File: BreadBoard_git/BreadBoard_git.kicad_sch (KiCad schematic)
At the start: 51 parts, among them IC1 IAUCN04S7L028ATMA1, J1 24V DC wall plug-iN, J2 LCD Driver, J3 Conn_01x15_Socket, Q1 CSD18512Q5B, Q2 CSD18512Q5B, Q3 RQ3E110AJTB, Q4 RQ3E110AJTB, Q5 RQ3E110AJTB, U1 ESP32-S3, U2 LM73605RNPR, U3 LM5148RGYR, U4 SHT45, U5 CSD17577Q5A, U6 ESP32-S3-WROOM-1

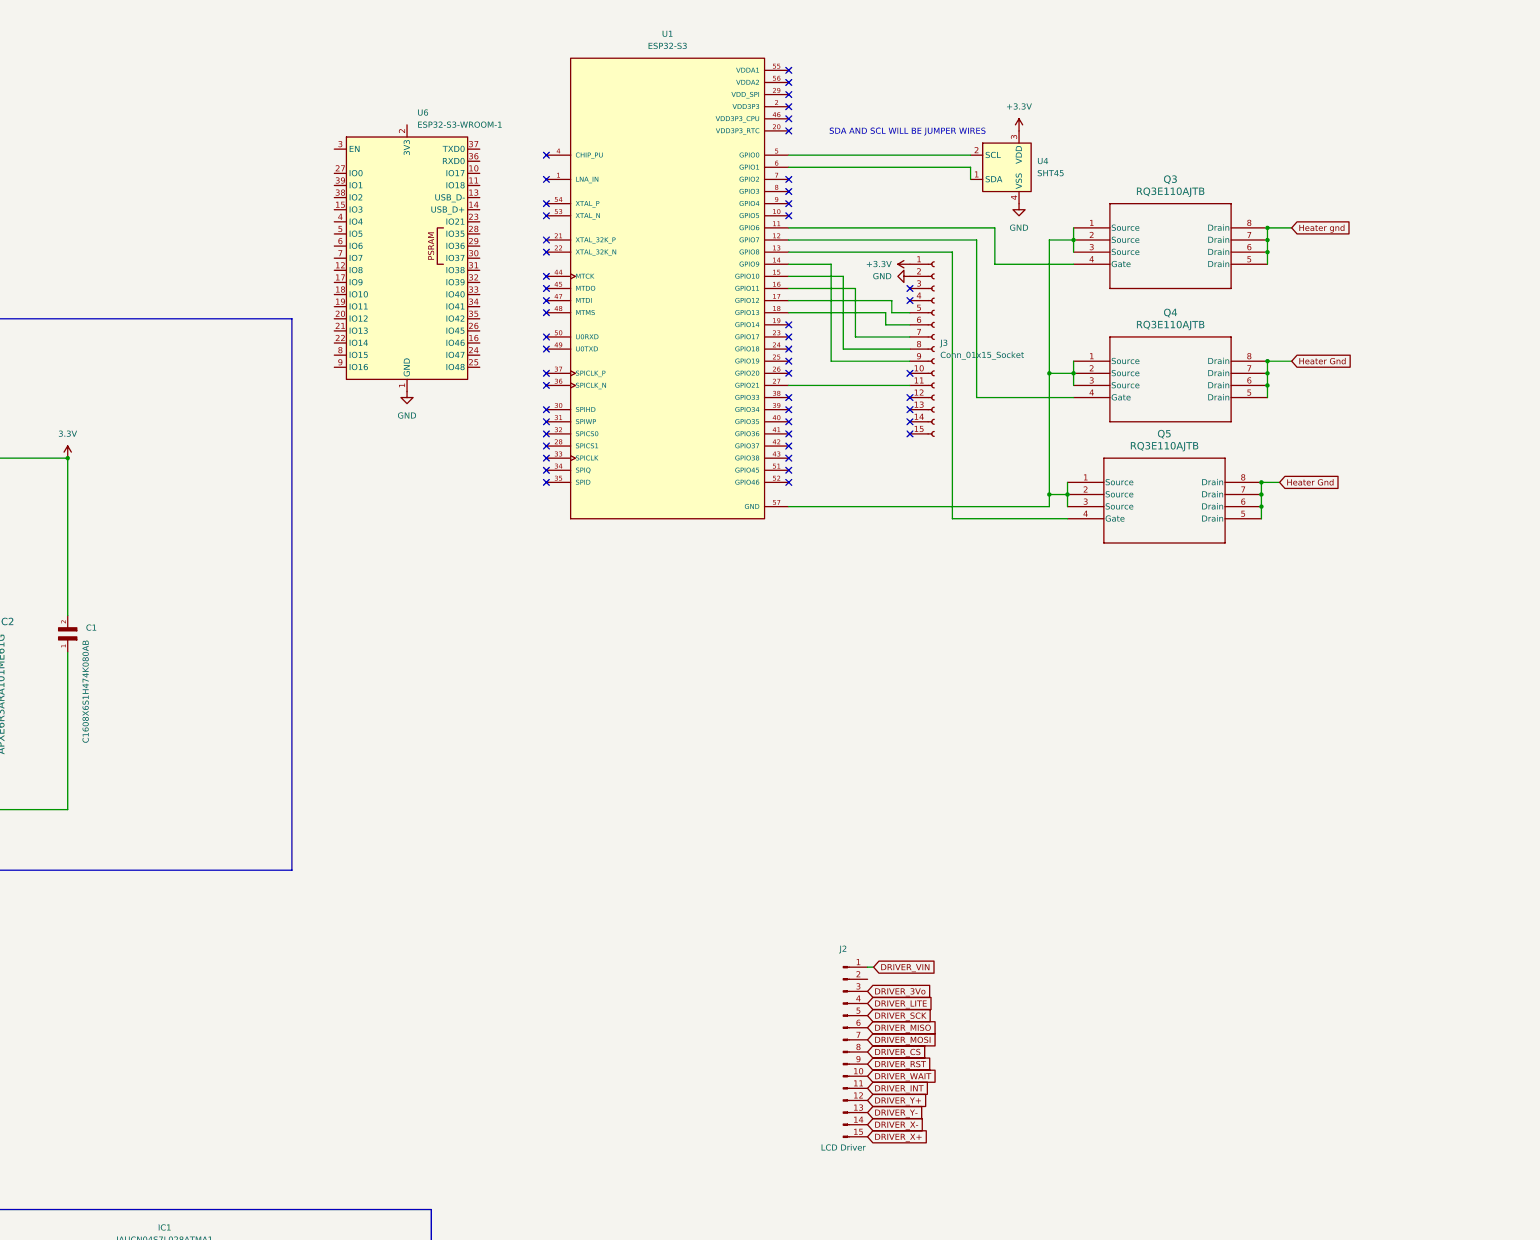
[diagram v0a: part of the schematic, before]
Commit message: 5V needs to be added
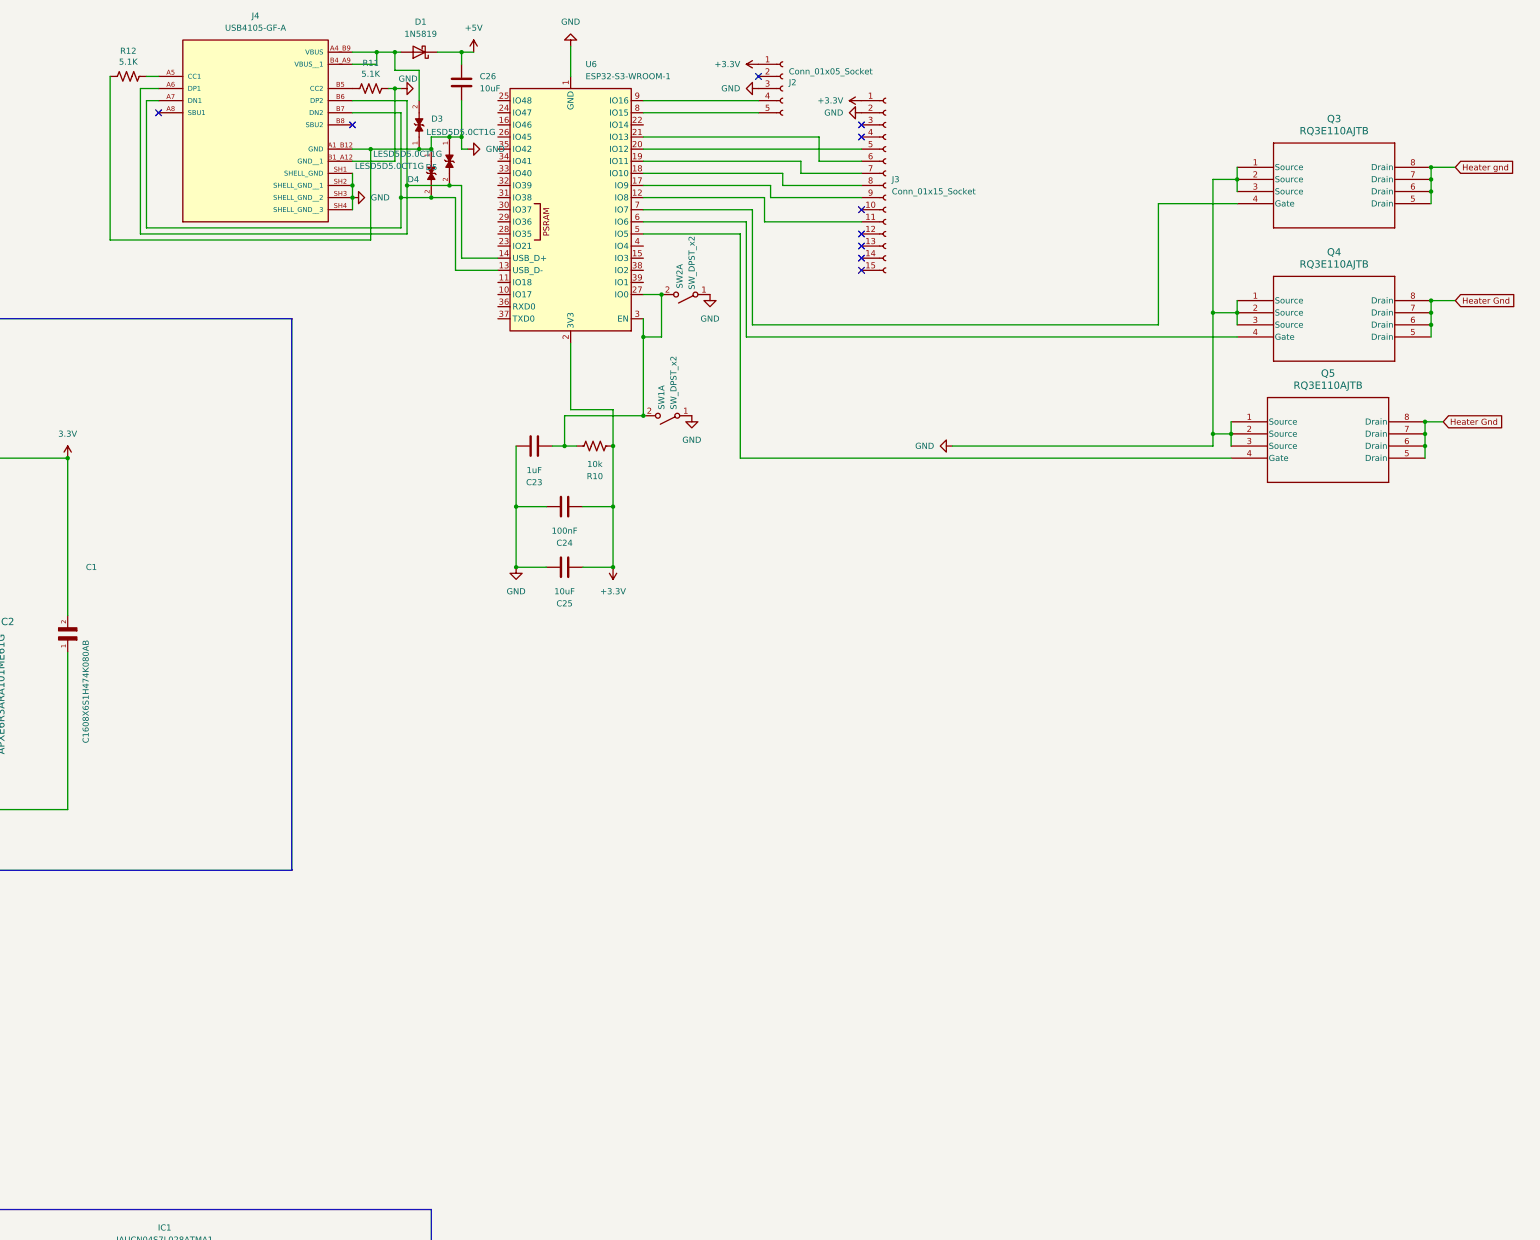
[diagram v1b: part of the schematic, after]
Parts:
- removed J2: LCD Driver, symbol Connector:Conn_01x15_Pin
- removed U1: ESP32-S3, ESP32-S3:IC_ESP32-S3, symbol ESP32-S3:ESP32-S3
- removed U4: SHT45, Sensor_Humidity:Sensirion_DFN-4_1.5x1.5mm_P0.8mm_SHT4x_NoCentralPad, symbol Sensor_Humidity:SHT4x
- added C23: 1uF, symbol Device:C
- added C24: 100nF, symbol Device:C
- added C25, C26: 10uF, symbol Device:C
- added D1: 1N5819, Diode_THT:D_DO-41_SOD81_P10.16mm_Horizontal, symbol Diode:1N5819
- added D3, D4, D5: LESD5D5.0CT1G, LESD5D5.0CT1G:TVS_LESD5D5.0CT1G, symbol LESD5D5.0CT1G:LESD5D5.0CT1G
- added J2: Conn_01x05_Socket, symbol Connector:Conn_01x05_Socket
- added J4: USB4105-GF-A, USB4105-GF-A:GCT_USB4105-GF-A, symbol USB4105-GF-A:USB4105-GF-A
- added R10: 10k, symbol Device:R_US
- added R11, R12: 5.1K, symbol Device:R_US
- added SW1, SW2: SW_DPST_x2, symbol Switch:SW_DPST_x2
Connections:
- net +3.3V: now also U6.2 (3V3), C24.1, C25.1, J2.1 (Pin_1), R10.2
- net DAP: now also Q3.1 (Source), Q3.2 (Source), Q3.3 (Source), Q4.1 (Source), Q4.2 (Source), Q4.3 (Source), Q5.1 (Source), Q5.2 (Source), Q5.3 (Source), C23.2, C24.2, C25.2, C26.2, D3.1, D4.1, D5.1, J2.3 (Pin_3), J4.A1_B12 (GND), J4.B1_A12 (GND__1), J4.SH1 (SHELL_GND), J4.SH2 (SHELL_GND__1), J4.SH3 (SHELL_GND__2), J4.SH4 (SHELL_GND__3), R11.2, R12.1, SW1.1 (A), SW2.1 (A)
- net at Q4.4 (Gate): now also U6.6 (IO6)
- net at Q5.4 (Gate): now also U6.5 (IO5)
- net at Q3.4 (Gate): now also U6.7 (IO7)
- net at J3.9 (Pin_9): now also U6.17 (IO9)
- net at J3.8 (Pin_8): now also U6.18 (IO10)
- net at J3.7 (Pin_7): now also U6.19 (IO11)
- net at J3.5 (Pin_5): now also U6.20 (IO12)
- net at J3.6 (Pin_6): now also U6.21 (IO13)
- net at J3.11 (Pin_11): now also U6.12 (IO8)
- net at U6.13 (USB_D-): now also D4.2, J4.A7 (DN1), J4.B7 (DN2)
- net at U6.14 (USB_D+): now also D5.2, J4.A6 (DP1), J4.B6 (DP2)
- net at U6.27 (IO0): now also U6.3 (EN), C23.1, R10.1, SW1.2 (B), SW2.2 (B)
- net at U6.8 (IO15): now also J2.5 (Pin_5)
- net at U6.9 (IO16): now also J2.4 (Pin_4)
- new net: J4.B5 (CC2), R11.1
- new net: D1.2 (A), D3.2, J4.A4_B9 (VBUS), J4.B4_A9 (VBUS__1)
- new net: J4.A5 (CC1), R12.2
- new net +5V: C26.1, D1.1 (K)
- no-connect marks 53 -> 12
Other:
- note removed: "SDA AND SCL WILL BE JUMPER WIRES"
- moved on the sheet: J3, Q3, Q4, Q5, U6

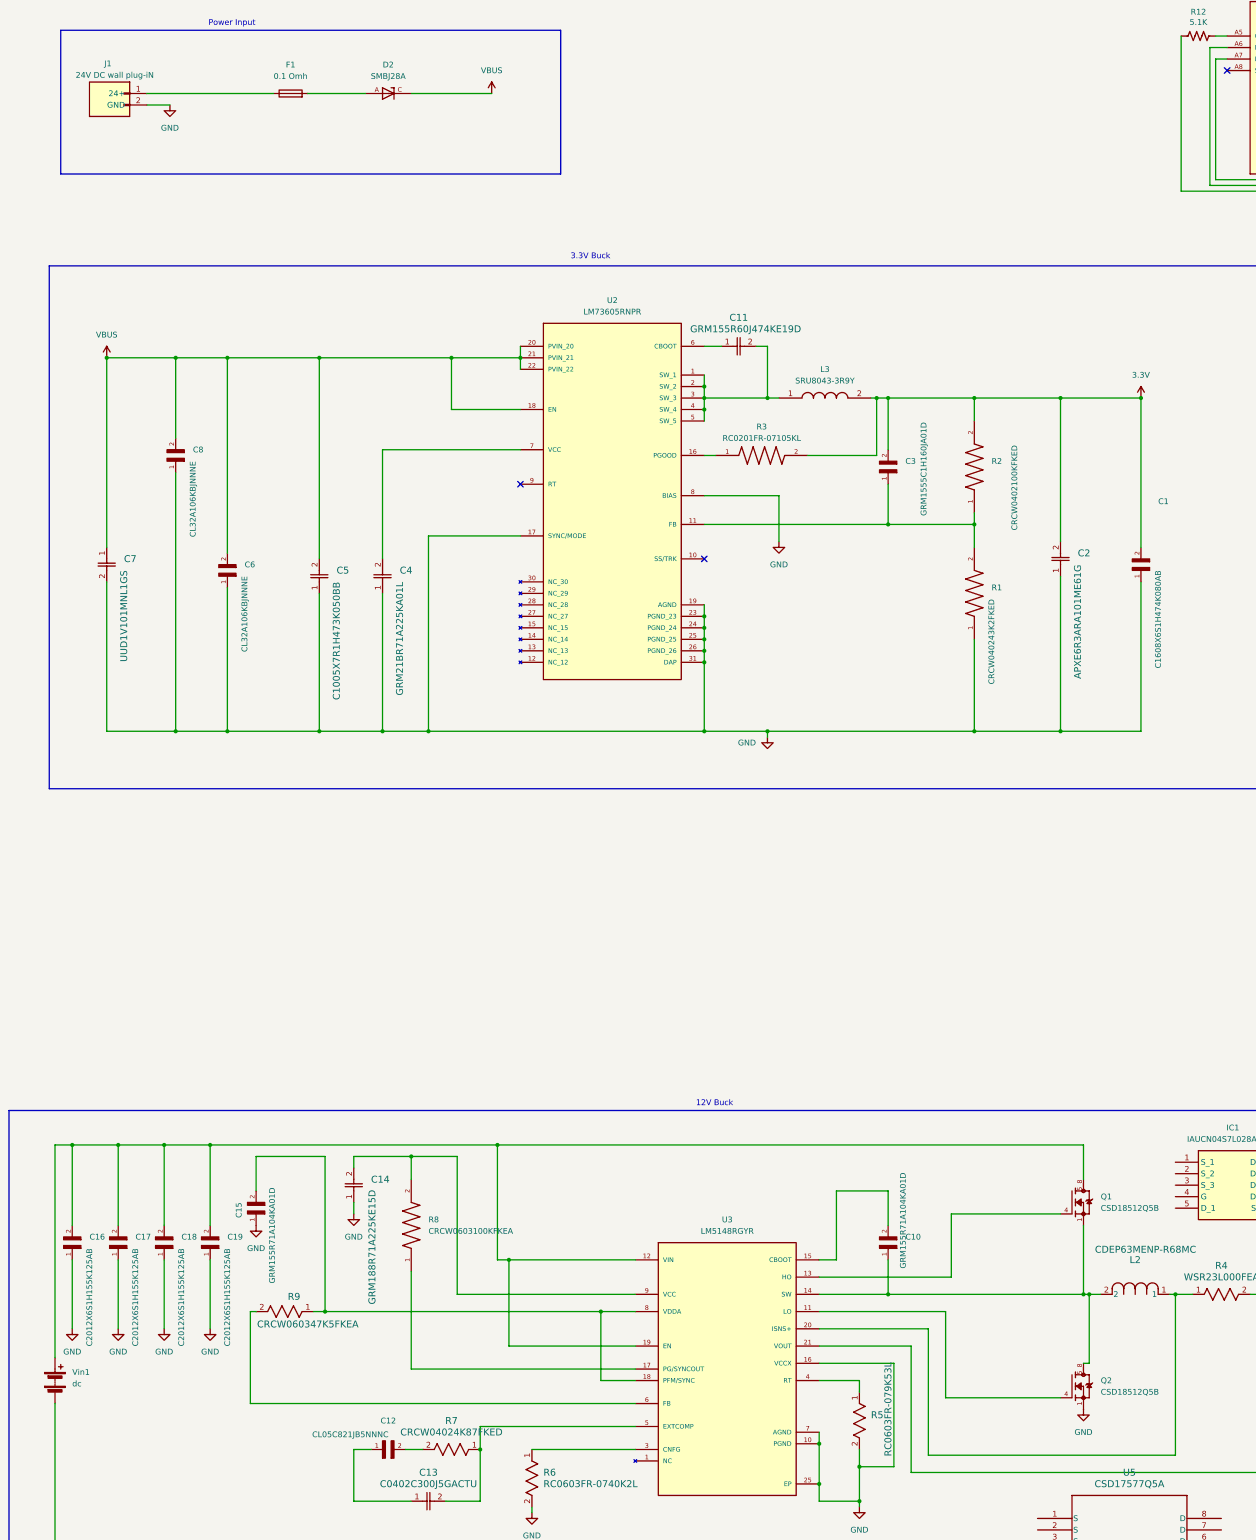
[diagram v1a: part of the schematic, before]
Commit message: most footprints in
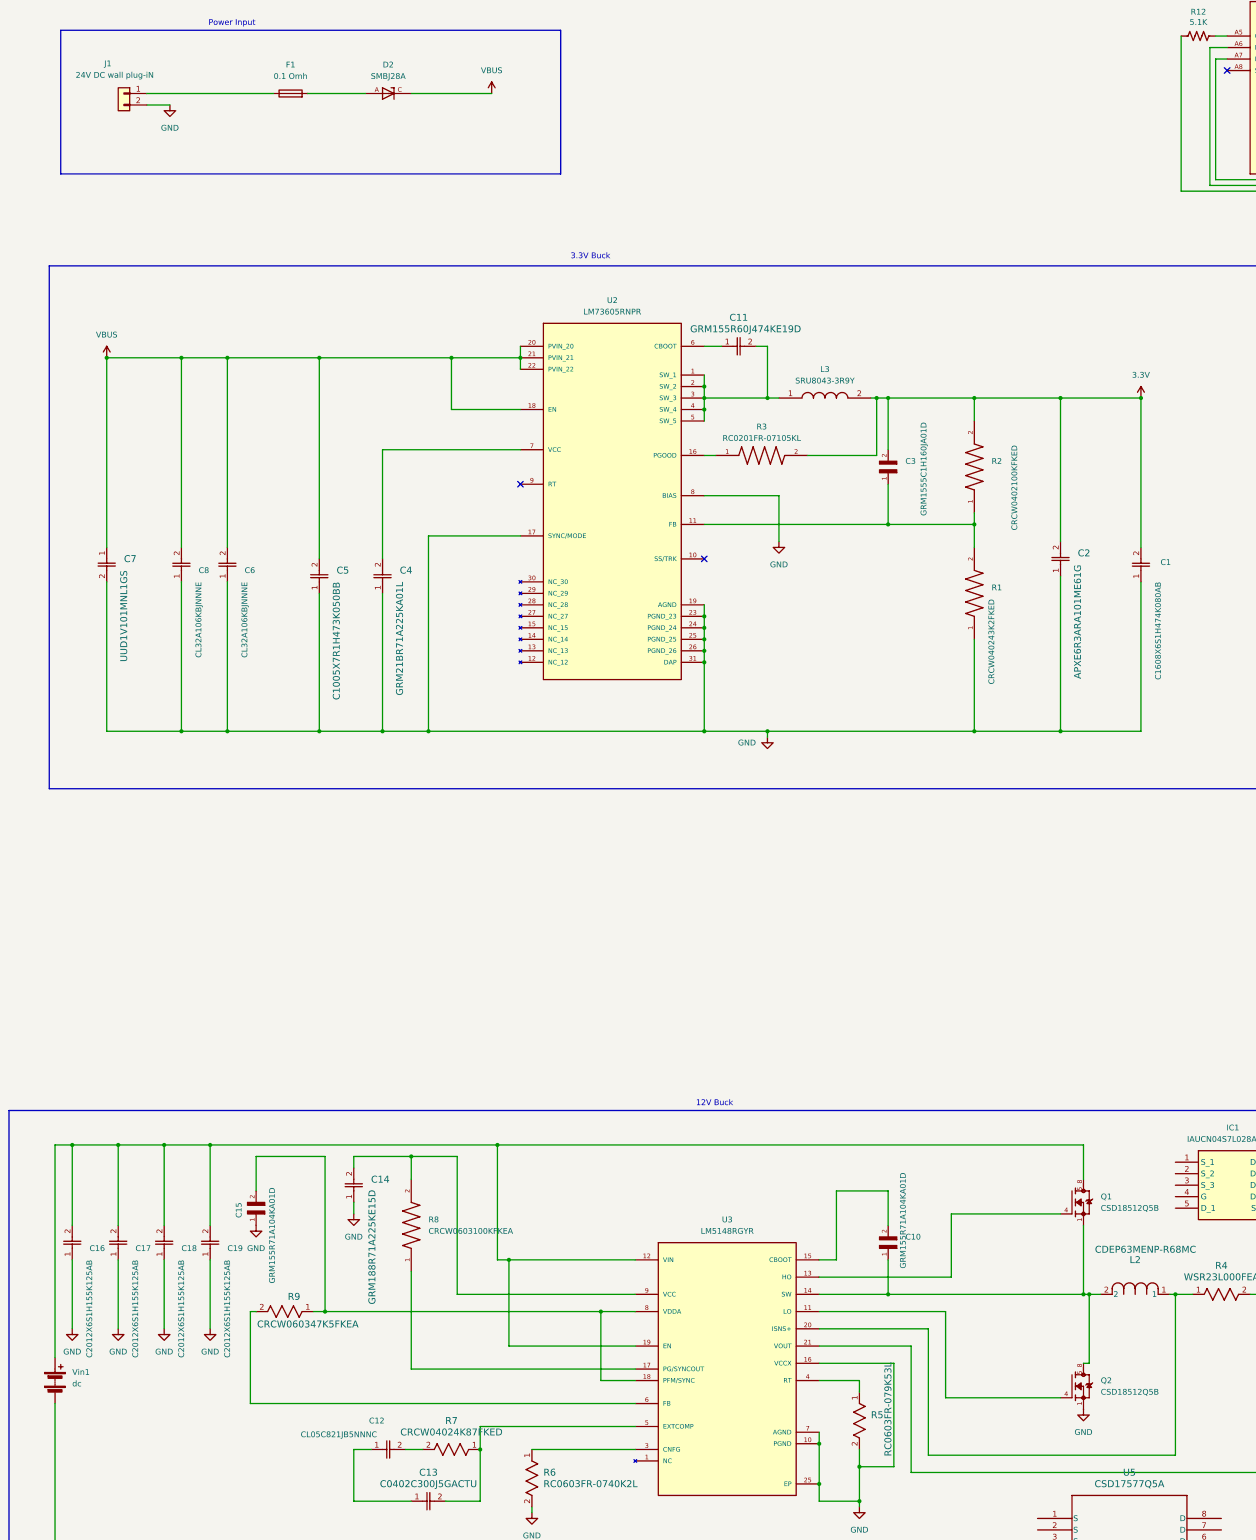
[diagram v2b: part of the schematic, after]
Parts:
- C1: footprint C1608X6S1H474K080AB:CAPC1608X90N -> CAP_1608_TDK
- C10, C15: footprint GRM155R71A104KA01D:CAPC1005X55N -> cvdda_5:CAPC1005X55N
- C12: footprint CL05C821JB5NNNC:CAPC1005X55N -> CAP_CL05_SAM
- C16, C17, C18, C19: footprint C2012X6S1H155K125AB:CAPC2012X145N -> CAP_2012_TDK
- C20, C21, C22, C9: footprint MSAST21GBB5106MTNA01:CAPC2012X145N -> cout_5:CAPC2012X145N
- C23, C24, C25, C26: footprint (none) -> Capacitor_SMD:C_0603_1608Metric
- C3: footprint GRM1555C1H160JA01D:CAPC1005X55N -> cff:CAPC1005X55N
- C6, C8: footprint CL32A106KBJNNNE:CAPC3225X270N -> CAP_CL32_SAM
- D3, D4, D5: footprint LESD5D5.0CT1G:TVS_LESD5D5.0CT1G -> led:TVS_LESD5D5.0CT1G
- J2: footprint (none) -> Connector_PinSocket_2.54mm:PinSocket_1x05_P2.54mm_Vertical
- J3: footprint (none) -> Connector_PinSocket_2.54mm:PinSocket_1x15_P2.54mm_Vertical
- J4: footprint USB4105-GF-A:GCT_USB4105-GF-A -> usb:GCT_USB4105-GF-A
- R1: footprint CRCW040243K2FKED:RESC1005X40N -> rfbb:RES_CRCW_0402
- R10, R11, R12: footprint (none) -> Resistor_SMD:R_0201_0603Metric
- R2: footprint CRCW0402100KFKED:RESC1005X40N -> rcomp_5:RES_CRCW_0402
- R3: footprint RC0201FR-07105KL:RESC0603X26N -> rpgood:RESC0603X26N
- R8: footprint CRCW0603100KFKEA:RESC1508X50N -> rpg_5:RES_CRCW_0603_VIS
- SW1, SW2: footprint (none) -> Button_Switch_SMD:SW_MEC_5GSH9
- U2: footprint LM73605RNPR:QFN50P600X400X80-31N -> LM7:QFN50P600X400X80-31N
- U3: footprint LM5148RGYR:QFN50P550X350X100-25N -> LM5:QFN50P550X350X100-25N
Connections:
- net VBUS: now reaches D2.C
- net VBUS: now also C5.2, C6.2, C7.1, C8.2, U2.18 (EN), U2.20 (PVIN_20), U2.21 (PVIN_21), U2.22 (PVIN_22)
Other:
- moved on the sheet: C6, C8
